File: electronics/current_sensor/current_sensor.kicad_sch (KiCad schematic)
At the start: 20 parts, among them J1 CS connector, J2 External connector, U1 INA253A3IPWR, U2 AD7685CRMZ, U3 ADR435BRMZ, U4 ADP7104ARDZ-5.0-R7, U5 ADP7104ARDZ-9.0-R7

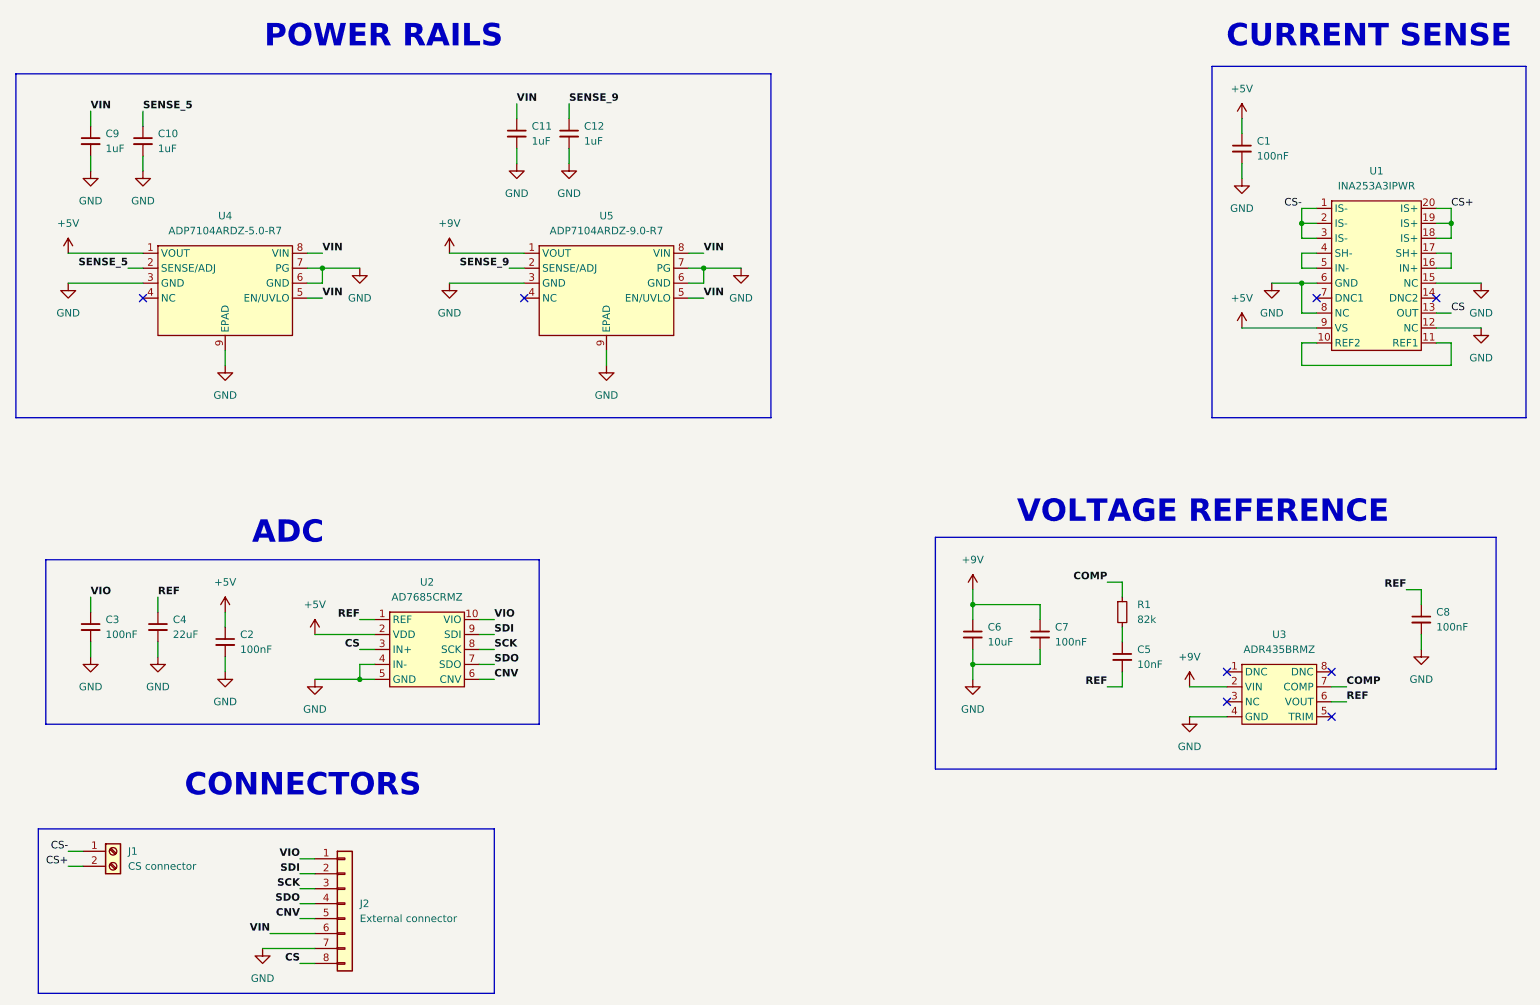
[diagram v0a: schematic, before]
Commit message: Update - Need to improve Storage class, very messy
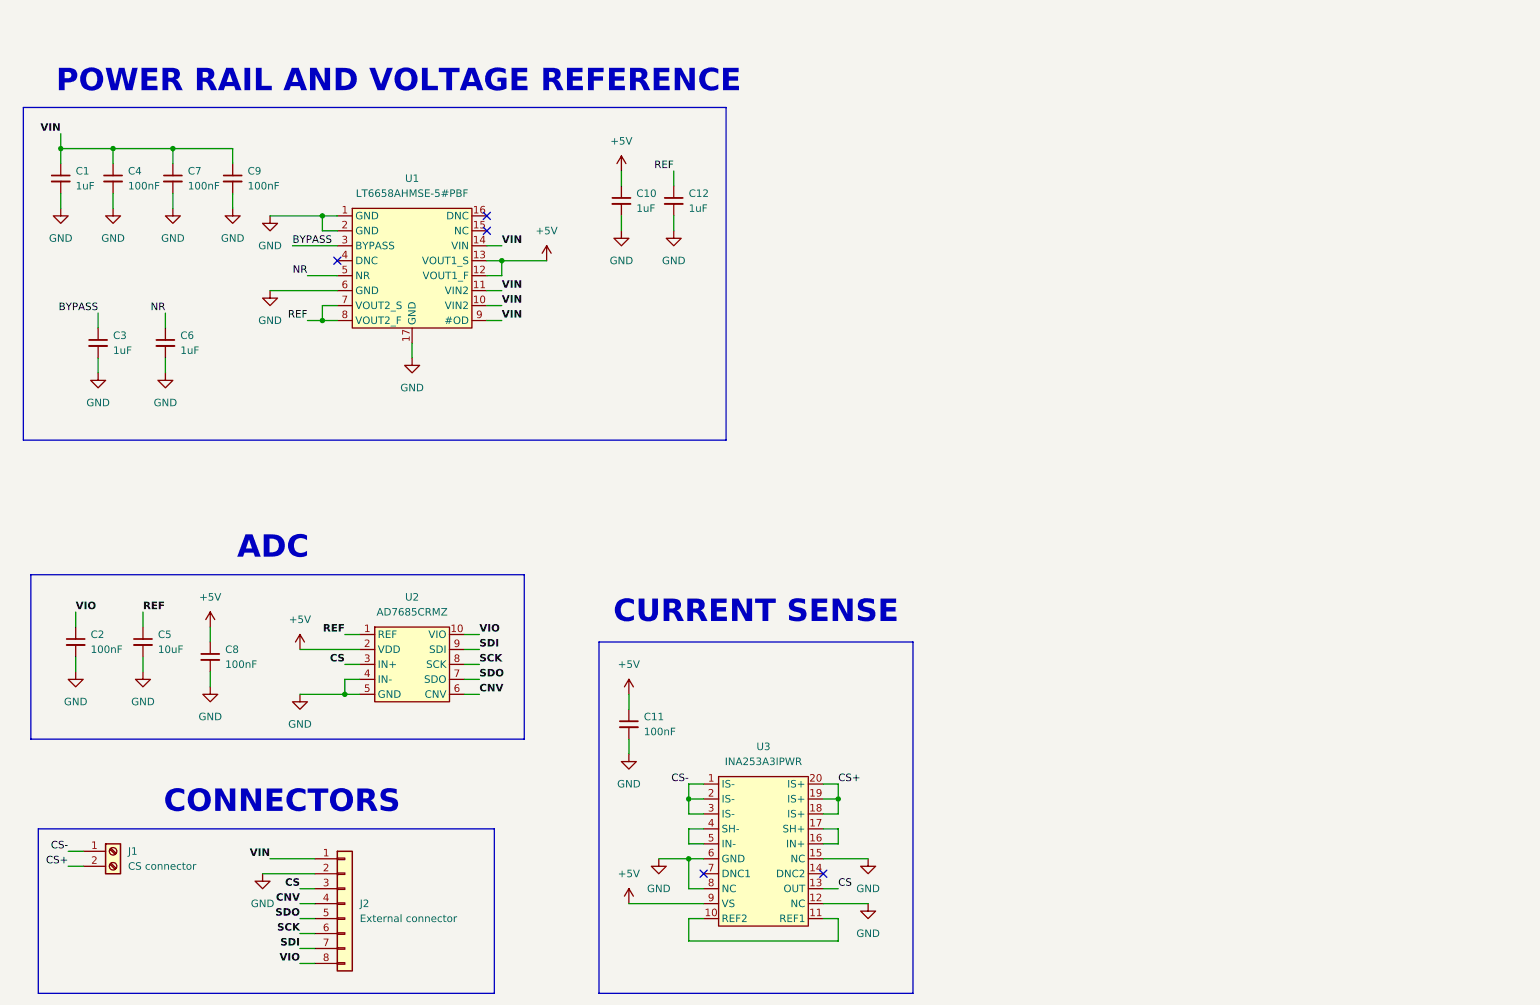
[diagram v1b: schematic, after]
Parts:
- removed C1, C2: 100nF, Capacitor_SMD:C_1206_3216Metric_Pad1.33x1.80mm_HandSolder, symbol Device:C_Small
- removed C5: 10nF, Capacitor_SMD:C_1206_3216Metric_Pad1.33x1.80mm_HandSolder, symbol Device:C_Small
- removed R1: 82k, Resistor_SMD:R_1206_3216Metric_Pad1.30x1.75mm_HandSolder, symbol Device:R_Small
- removed U3: ADR435BRMZ, Package_SO:MSOP-8_3x3mm_P0.65mm, symbol 0_servo:ADR435BRMZ
- removed U4: ADP7104ARDZ-5.0-R7, Package_SO:SOIC-8-1EP_3.9x4.9mm_P1.27mm_EP2.41x3.81mm, symbol 0_servo:ADP7104ARDZ-5.0-R7
- removed U5: ADP7104ARDZ-9.0-R7, Package_SO:SOIC-8-1EP_3.9x4.9mm_P1.27mm_EP2.41x3.81mm, symbol 0_servo:ADP7104ARDZ-9.0-R7
- added C3: 1uF, Capacitor_SMD:C_0805_2012Metric_Pad1.18x1.45mm_HandSolder, symbol Device:C_Small
- added C4, C9: 100nF, Capacitor_SMD:C_0805_2012Metric_Pad1.18x1.45mm_HandSolder, symbol Device:C_Small
- added U1: LT6658AHMSE-5#PBF, Package_SO:MSOP-16-1EP_3x4.039mm_P0.5mm_EP1.651x2.845mm, symbol 0_servo:LT6658AHMSE-5#PBF
- C10, C12, C7, C8: footprint Capacitor_SMD:C_1206_3216Metric_Pad1.33x1.80mm_HandSolder -> Capacitor_SMD:C_0805_2012Metric_Pad1.18x1.45mm_HandSolder
- C11: value 1uF -> 100nF; footprint Capacitor_SMD:C_1206_3216Metric_Pad1.33x1.80mm_HandSolder -> Capacitor_SMD:C_0805_2012Metric_Pad1.18x1.45mm_HandSolder
- C2: renamed from C3; footprint Capacitor_SMD:C_1206_3216Metric_Pad1.33x1.80mm_HandSolder -> Capacitor_SMD:C_0805_2012Metric_Pad1.18x1.45mm_HandSolder
- C5: renamed from C4; value 22uF -> 10uF; footprint Capacitor_SMD:C_1206_3216Metric_Pad1.33x1.80mm_HandSolder -> Capacitor_SMD:C_0805_2012Metric_Pad1.18x1.45mm_HandSolder
- C6: value 10uF -> 1uF; footprint Capacitor_SMD:C_1206_3216Metric_Pad1.33x1.80mm_HandSolder -> Capacitor_SMD:C_0805_2012Metric_Pad1.18x1.45mm_HandSolder
- renumbered C9 to C1, U1 to U3
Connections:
- net SENSE_5 is gone; now on net +5V: C10.1
- net SENSE_9 is gone; now on net REF: C12.1
- net +5V: now also C11.1, C8.1, U1.12 (VOUT1_F), U1.13 (VOUT1_S)
- net CNV: now also J2.4 (Pin_4); no longer J2.5 (Pin_5)
- net CS: now also J2.3 (Pin_3); no longer J2.8 (Pin_8)
- net GND: now also J2.2 (Pin_2), C3.2, C4.2, C9.2, U1.1 (GND), U1.17 (GND), U1.2 (GND), U1.6 (GND); no longer J2.7 (Pin_7)
- net REF: now also U1.7 (VOUT2_S), U1.8 (VOUT2_F); no longer C8.1
- net SCK: now also J2.6 (Pin_6); no longer J2.3 (Pin_3)
- net SDI: now also J2.7 (Pin_7); no longer J2.2 (Pin_2)
- net SDO: now also J2.5 (Pin_5); no longer J2.4 (Pin_4)
- net VIN: now also C7.1, J2.1 (Pin_1), C4.1, C9.1, U1.10 (VIN2), U1.11 (VIN2), U1.14 (VIN), U1.9 (#OD); no longer C11.1, J2.6 (Pin_6)
- net VIO: now also J2.8 (Pin_8); no longer J2.1 (Pin_1)
- net +9V renamed NR
- net NR: now also U1.5 (NR); no longer C7.1
- new net BYPASS: C3.1, U1.3 (BYPASS)
- no-connect marks 8 -> 5
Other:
- note added: "POWER RAIL AND VOLTAGE REFERENCE"
- note removed: "POWER RAILS"
- note removed: "VOLTAGE REFERENCE"
- moved on the sheet: C1, C2, C5, U2, U3
